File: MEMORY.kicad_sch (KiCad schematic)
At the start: 2 parts, among them IC1 ECP5-BGA256, U6 S27KL0641

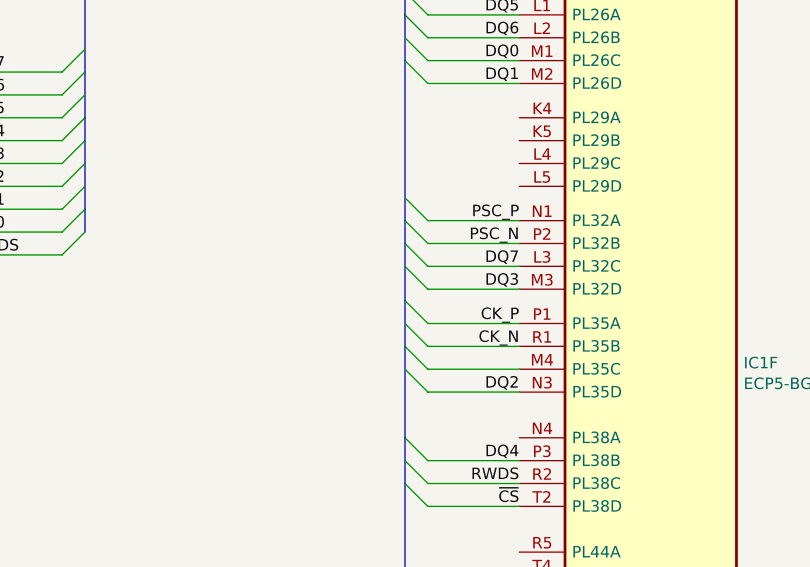
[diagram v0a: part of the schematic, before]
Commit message: Add semi-critical resistor values
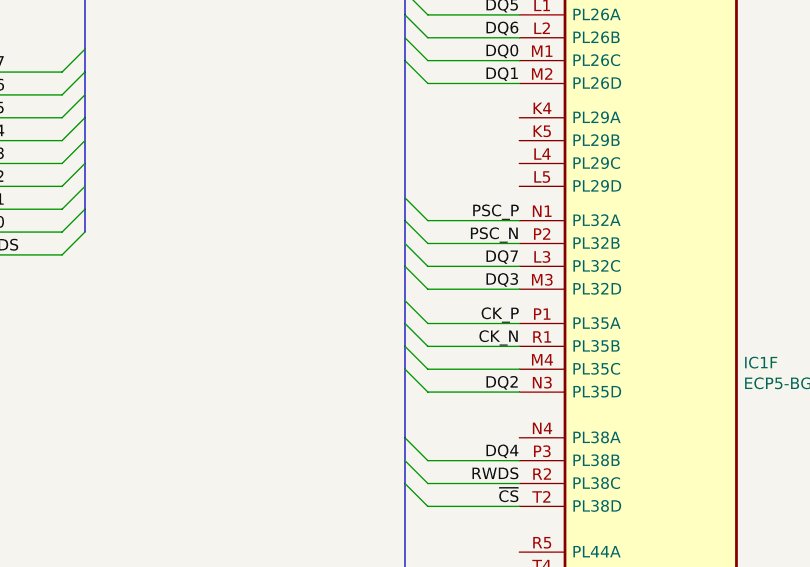
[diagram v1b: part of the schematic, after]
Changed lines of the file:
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@@
-(kicad_sch (version 20200618) (host eeschema "5.99.0-unknown-7340c97~102~ubuntu20.04.1")
-  (page 3 6)
+(kicad_sch (version 20200618) (host eeschema "5.99.0-unknown-e9da02e~102~ubuntu20.04.1")
+  (page 1 6)
   (paper "A4")
   (bus_alias "HYPERRAM" (members "DQ[0..7]" "RWDS" "~CS" "CK_N" "CK_P" "PSC_N" "PSC_P" "~RESET"))
@@
   (junction (at 151.765 52.705) (diameter 0) (color 0 0 0 0))
   (no_connect (at 139.065 92.71))
+  (no_connect (at 139.065 87.63))
   (no_connect (at 139.065 90.17))
-  (no_connect (at 139.065 87.63))
   (bus_entry (at 97.155 69.85) (size 2.54 -2.54)
     (stroke (width 0.1524) (type solid) (color 0 0 0 0))
@@
     (stroke (width 0) (type solid) (color 0 0 0 0))
   )
-  (bus (pts (xy 187.325 78.74) (xy 187.325 81.28))
-    (stroke (width 0) (type solid) (color 0 0 0 0))
-  )
-  (bus (pts (xy 187.325 81.28) (xy 187.325 87.63))
-    (stroke (width 0) (type solid) (color 0 0 0 0))
-  )
-  (bus (pts (xy 187.325 87.63) (xy 187.325 92.71))
-    (stroke (width 0) (type solid) (color 0 0 0 0))
-  )
+  (bus (pts (xy 187.325 78.74) (xy 187.325 83.82))
+    (stroke (width 0) (type solid) (color 0 0 0 0))
+  )
+  (bus (pts (xy 187.325 83.82) (xy 187.325 90.17))
+    (stroke (width 0) (type solid) (color 0 0 0 0))
+  )
+  (bus (pts (xy 187.325 90.17) (xy 187.325 92.71))
+    (stroke (width 0) (type solid) (color 0 0 0 0))
+  )

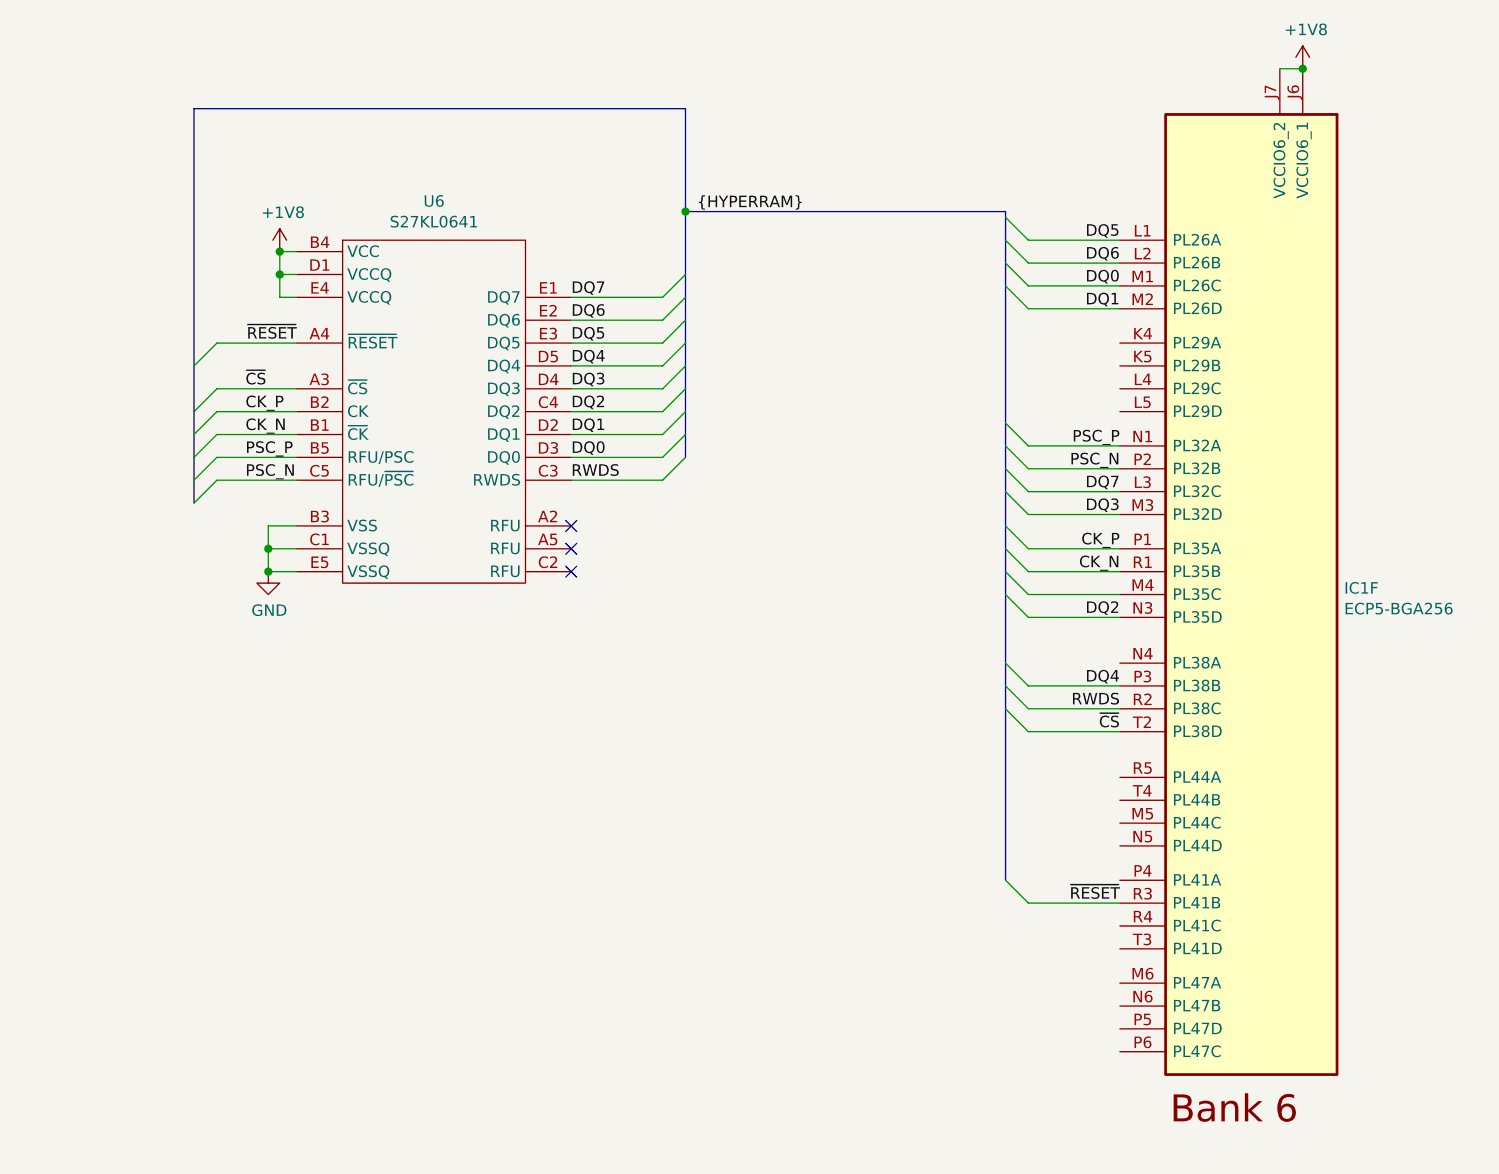
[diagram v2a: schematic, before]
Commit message: Change oscillator to SI5315, change RGB LED
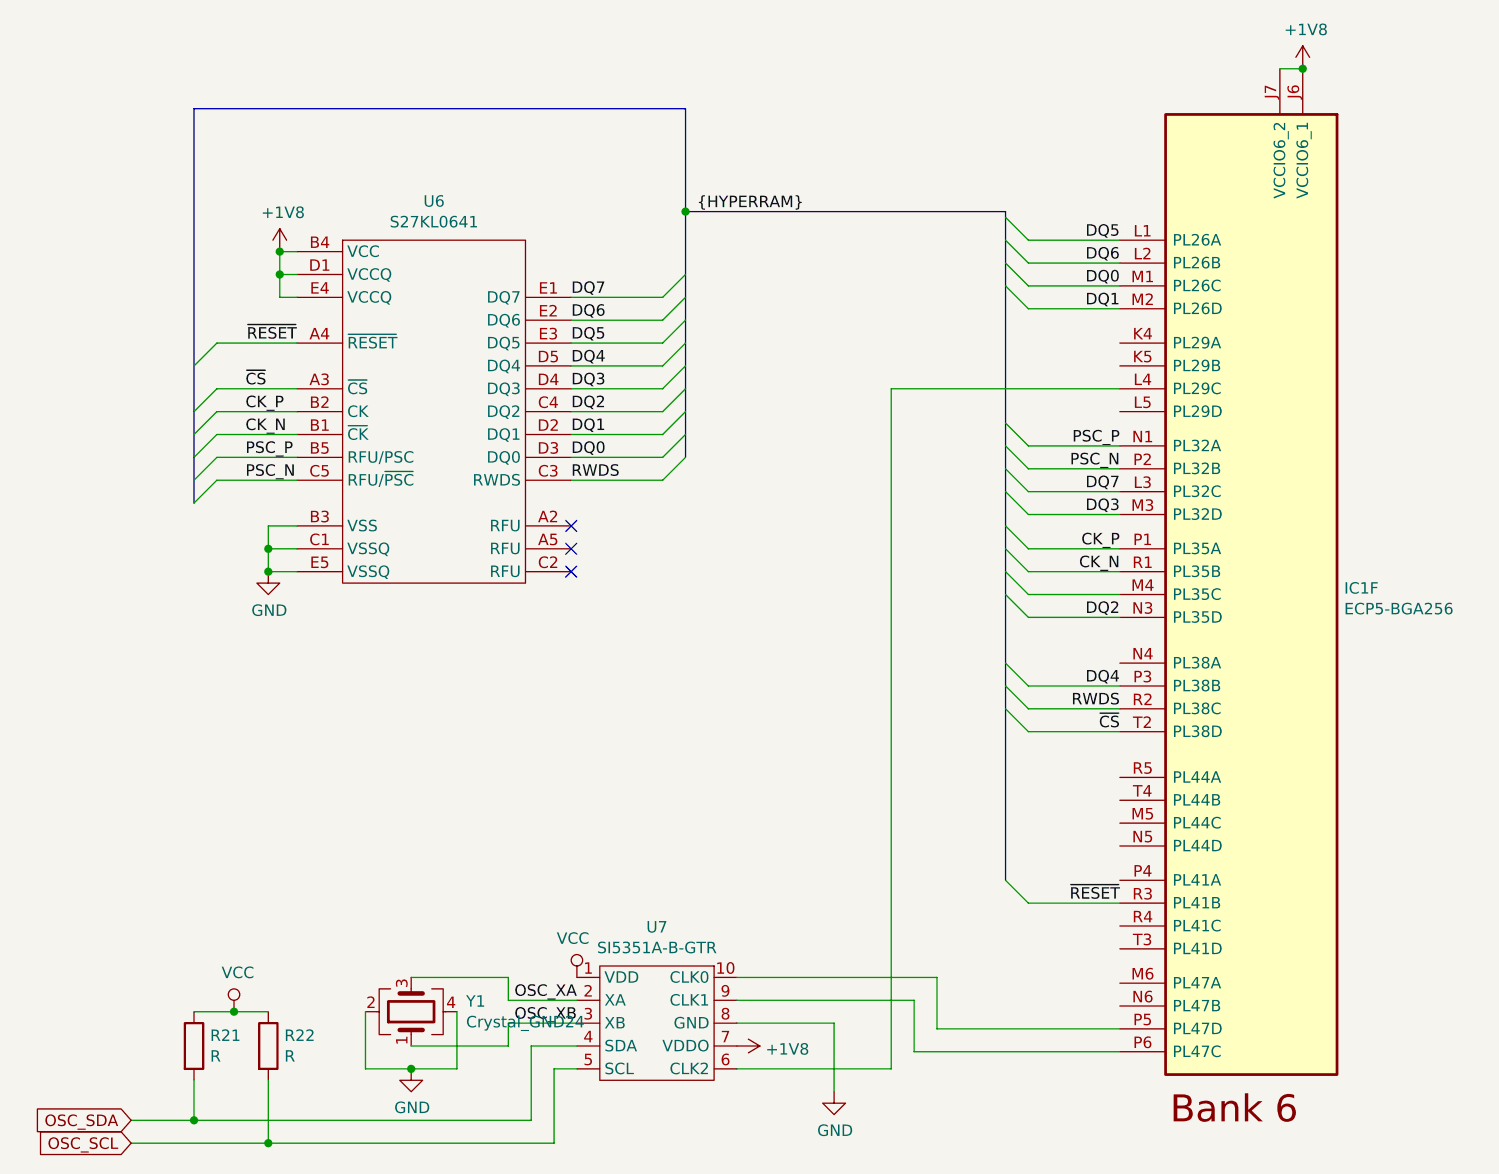
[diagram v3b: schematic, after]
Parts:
- added R21, R22: R, Resistor_SMD:R_0402_1005Metric, symbol Device:R
- added U7: SI5351A-B-GTR, Package_SO:MSOP-10_3x3mm_P0.5mm, symbol mini_mipi:SI5351A-B-GTR
- added Y1: Crystal_GND24, Crystal:Crystal_SMD_2016-4Pin_2.0x1.6mm, symbol Device:Crystal_GND24
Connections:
- net +1V8: now also U7.7 (VDDO)
- net GND: now also U7.8 (GND), Y1.2, Y1.4
- net at IC1.L4 (PL29C): now also U7.6 (CLK2)
- net at IC1.P5 (PL47D): now also U7.10 (CLK0)
- net at IC1.P6 (PL47C): now also U7.9 (CLK1)
- new net OSC_SCL: R22.2, U7.5 (SCL)
- new net OSC_SDA: R21.2, U7.4 (SDA)
- new net OSC_XA: U7.2 (XA), Y1.3
- new net OSC_XB: U7.3 (XB), Y1.1
- new net VCC: R21.1, R22.1, U7.1 (VDD)
